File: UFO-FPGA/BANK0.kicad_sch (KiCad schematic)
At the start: 7 parts, among them U1 ICE40HX8K-BG121

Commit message: PCB
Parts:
- TP8: footprint TestPoint:TestPoint_Keystone_5000-5004_Miniature -> TestPoint:TestPoint_Pad_1.5x1.5mm
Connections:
- net ADC-CS: no longer U1.A5 (IOT_207)
- net MISO: no longer U1.A4 (IOT_211)
- net PIN-1: no longer U1.A1 (IOT_225)
- net PIN-2: no longer U1.A3 (IOT_223)
- net PIN-3: no longer U1.A2 (IOT_222)
- net PIN-4: no longer U1.B3 (IOT_221)
- net PIN-5: no longer U1.B4 (IOT_219)
- net PIN-6: no longer U1.B6 (IOT_198_GBIN0)
- net PIN-7: no longer U1.B7 (IOT_197_GBIN1)
- net SCK: no longer U1.A6 (IOT_206)
- net +1V2 renamed +3V3
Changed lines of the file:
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@@
+    (stroke (width 0) (type default))
+  )
+  (wire (pts (xy 191.135 48.895) (xy 191.135 38.735))
     (stroke (width 0) (type default))
   )
@@
     (stroke (width 0) (type default))
   )
+  (wire (pts (xy 101.6 108.585) (xy 114.3 108.585))
+    (stroke (width 0) (type default))
+  )
   (wire (pts (xy 127 48.895) (xy 127 57.785))
     (stroke (width 0) (type default))
   )
-  (wire (pts (xy 101.6 108.585) (xy 114.3 108.585))
-    (stroke (width 0) (type default))
-  )
   (wire (pts (xy 160.02 56.515) (xy 148.59 56.515))
     (stroke (width 0) (type default))
@@
     (stroke (width 0) (type default))
   )
-  (wire (pts (xy 190.5 38.735) (xy 190.5 48.895))
+  (wire (pts (xy 190.5 48.895) (xy 191.135 48.895))
     (stroke (width 0) (type default))
   )
@@
     (effects (font (size 1.27 1.27)) (justify left bottom))
   )
-  (global_label "PIN-7" (shape input) (at 101.6 100.965 180) (fields_autoplaced)
-    (effects (font (size 1.27 1.27)) (justify right))
-    (property "Intersheetrefs" "${INTERSHEET_REFS}" (at 92.707 100.965 0)
-      (effects (font (size 1.27 1.27)) (justify right) hide)
-    )
-  )
-  (global_label "PIN-3" (shape input) (at 101.6 123.825 180) (fields_autoplaced)
-    (effects (font (size 1.27 1.27)) (justify right))
-    (property "Intersheetrefs" "${INTERSHEET_REFS}" (at 92.707 123.825 0)
-      (effects (font (size 1.27 1.27)) (justify right) hide)
-    )
-  )
-  (global_label "PIN-6" (shape input) (at 101.6 103.505 180) (fields_autoplaced)
-    (effects (font (size 1.27 1.27)) (justify right))
-    (property "Intersheetrefs" "${INTERSHEET_REFS}" (at 92.707 103.505 0)
-      (effects (font (size 1.27 1.27)) (justify right) hide)
-    )
-  )
-  (global_label "MISO" (shape input) (at 101.6 113.665 180) (fields_autoplaced)
-    (effects (font (size 1.27 1.27)) (justify right))
-    (property "Intersheetrefs" "${INTERSHEET_REFS}" (at 94.098 113.665 0)
-      (effects (font (size 1.27 1.27)) (justify right) hide)
-    )
-  )
-  (global_label "ADC-CS" (shape input) (at 101.6 108.585 180) (fields_autoplaced)
-    (effects (font (size 1.27 1.27)) (justify right))
-    (property "Intersheetrefs" "${INTERSHEET_REFS}" (at 91.0137 108.585 0)
-      (effects (font (size 1.27 1.27)) (justify right) hide)
-    )
-  )
-  (global_label "PIN-5" (shape input) (at 101.6 118.745 180) (fields_autoplaced)
-    (effects (font (size 1.27 1.27)) (justify right))
-    (property "Intersheetrefs" "${INTERSHEET_REFS}" (at 92.707 118.745 0)
-      (effects (font (size 1.27 1.27)) (justify right) hide)
-    )
-  )
-  (global_label "PIN-2" (shape input) (at 101.6 126.365 180) (fields_autoplaced)
-    (effects (font (size 1.27 1.27)) (justify right))
-    (property "Intersheetrefs" "${INTERSHEET_REFS}" (at 92.707 126.365 0)
-      (effects (font (size 1.27 1.27)) (justify right) hide)
-    )
-  )
-  (global_label "PIN-1" (shape input) (at 101.6 128.905 180) (fields_autoplaced)
-    (effects (font (size 1.27 1.27)) (justify right))
-    (property "Intersheetrefs" "${INTERSHEET_REFS}" (at 92.707 128.905 0)
-      (effects (font (size 1.27 1.27)) (justify right) hide)
-    )
-  )
-  (global_label "SCK" (shape input) (at 101.6 106.045 180) (fields_autoplaced)
-    (effects (font (size 1.27 1.27)) (justify right))
-    (property "Intersheetrefs" "${INTERSHEET_REFS}" (at 94.9447 106.045 0)
-      (effects (font (size 1.27 1.27)) (justify right) hide)
-    )
-  )
-  (global_label "PIN-4" (shape input) (at 101.6 121.285 180) (fields_autoplaced)
-    (effects (font (size 1.27 1.27)) (justify right))
-    (property "Intersheetrefs" "${INTERSHEET_REFS}" (at 92.707 121.285 0)
+  (global_label "PIN-7" (shape input) (at 92.71 100.965 180) (fields_autoplaced)
+    (effects (font (size 1.27 1.27)) (justify right))
+    (property "Intersheetrefs" "${INTERSHEET_REFS}" (at 83.817 100.965 0)
+      (effects (font (size 1.27 1.27)) (justify right) hide)
+    )
+  )
+  (global_label "PIN-3" (shape input) (at 92.71 123.825 180) (fields_autoplaced)
+    (effects (font (size 1.27 1.27)) (justify right))
+    (property "Intersheetrefs" "${INTERSHEET_REFS}" (at 83.817 123.825 0)
+      (effects (font (size 1.27 1.27)) (justify right) hide)
+    )
+  )
+  (global_label "PIN-6" (shape input) (at 92.71 103.505 180) (fields_autoplaced)
+    (effects (font (size 1.27 1.27)) (justify right))
+    (property "Intersheetrefs" "${INTERSHEET_REFS}" (at 83.817 103.505 0)
+      (effects (font (size 1.27 1.27)) (justify right) hide)
+    )
+  )
+  (global_label "MISO" (shape input) (at 92.71 113.665 180) (fields_autoplaced)
+    (effects (font (size 1.27 1.27)) (justify right))
+    (property "Intersheetrefs" "${INTERSHEET_REFS}" (at 85.208 113.665 0)
+      (effects (font (size 1.27 1.27)) (justify right) hide)
+    )
+  )
+  (global_label "ADC-CS" (shape input) (at 92.71 108.585 180) (fields_autoplaced)
+    (effects (font (size 1.27 1.27)) (justify right))
+    (property "Intersheetrefs" "${INTERSHEET_REFS}" (at 82.1237 108.585 0)
+      (effects (font (size 1.27 1.27)) (justify right) hide)
+    )
+  )
+  (global_label "PIN-5" (shape input) (at 92.71 118.745 180) (fields_autoplaced)
+    (effects (font (size 1.27 1.27)) (justify right))
+    (property "Intersheetrefs" "${INTERSHEET_REFS}" (at 83.817 118.745 0)
+      (effects (font (size 1.27 1.27)) (justify right) hide)
+    )
+  )
+  (global_label "PIN-2" (shape input) (at 92.71 126.365 180) (fields_autoplaced)
+    (effects (font (size 1.27 1.27)) (justify right))
+    (property "Intersheetrefs" "${INTERSHEET_REFS}" (at 83.817 126.365 0)
+      (effects (font (size 1.27 1.27)) (justify right) hide)
+    )
+  )
+  (global_label "PIN-1" (shape input) (at 92.71 128.905 180) (fields_autoplaced)
+    (effects (font (size 1.27 1.27)) (justify right))
+    (property "Intersheetrefs" "${INTERSHEET_REFS}" (at 83.817 128.905 0)
+      (effects (font (size 1.27 1.27)) (justify right) hide)
+    )
+  )
+  (global_label "SCK" (shape input) (at 92.71 106.045 180) (fields_autoplaced)
+    (effects (font (size 1.27 1.27)) (justify right))
+    (property "Intersheetrefs" "${INTERSHEET_REFS}" (at 86.0547 106.045 0)
+      (effects (font (size 1.27 1.27)) (justify right) hide)
+    )
+  )
+  (global_label "PIN-4" (shape input) (at 92.71 121.285 180) (fields_autoplaced)
+    (effects (font (size 1.27 1.27)) (justify right))
+    (property "Intersheetrefs" "${INTERSHEET_REFS}" (at 83.817 121.285 0)
       (effects (font (size 1.27 1.27)) (justify right) hide)
     )
@@
         (path "/de984c47-a4b3-4404-8f6d-5958f9d846d6"
           (reference "#PWR0101") (unit 1)
+        )
+      )
+    )
+  )
+  (symbol (lib_id "power:+3V3") (at 191.135 38.735 0) (unit 1)
+    (in_bom yes) (on_board yes) (dnp no) (fields_autoplaced)
+    (property "Reference" "#PWR062" (at 191.135 42.545 0)
+      (effects (font (size 1.27 1.27)) hide)
+    )
+    (property "Value" "+3V3" (at 191.135 35.2331 0)
+      (effects (font (size 1.27 1.27)))
+    )
+    (property "Footprint" "" (at 191.135 38.735 0)
+      (effects (font (size 1.27 1.27)) hide)
+    )
+    (property "Datasheet" "" (at 191.135 38.735 0)
+      (effects (font (size 1.27 1.27)) hide)
+    )
+    (pin "1")
+    (instances
+      (project "UFO-FPGA"
+        (path "/b3168f6a-c732-41d3-aeeb-d97dd2f1bb65/03eb349d-f783-448d-a9ad-735fd21dbf61"
+          (reference "#PWR062") (unit 1)
         )
       )
@@
     )
   )
-  (symbol (lib_id "power:+1V2") (at 190.5 38.735 0) (unit 1)
-    (in_bom yes) (on_board yes) (dnp no) (fields_autoplaced)
-    (property "Reference" "#PWR024" (at 190.5 42.545 0)
-      (effects (font (size 1.27 1.27)) hide)
-    )
-    (property "Value" "+1V2" (at 190.5 35.2331 0)
-      (effects (font (size 1.27 1.27)))
-    )
-    (property "Footprint" "" (at 190.5 38.735 0)
-      (effects (font (size 1.27 1.27)) hide)
-    )
-    (property "Datasheet" "" (at 190.5 38.735 0)
-      (effects (font (size 1.27 1.27)) hide)
-    )
-    (pin "1")
-    (instances
-      (project "UFO-FPGA"
-        (path "/b3168f6a-c732-41d3-aeeb-d97dd2f1bb65/a9a0295d-b075-4952-a5ba-04debc5f691c"
-          (reference "#PWR024") (unit 1)
-        )
-        (path "/b3168f6a-c732-41d3-aeeb-d97dd2f1bb65/03eb349d-f783-448d-a9ad-735fd21dbf61"
-          (reference "#PWR076") (unit 1)
-        )
-        (path "/b3168f6a-c732-41d3-aeeb-d97dd2f1bb65/6f7e0d88-d92b-4c4f-9dc8-64721cd46d41"
-          (reference "#PWR029") (unit 1)
-        )
-        (path "/b3168f6a-c732-41d3-aeeb-d97dd2f1bb65/f54d4357-d916-4d6b-afb9-9dd5f65d1cf7"
-          (reference "#PWR036") (unit 1)
-        )
-      )
-      (project "BANK0"
-        (path "/de984c47-a4b3-4404-8f6d-5958f9d846d6"
-          (reference "#PWR024") (unit 1)
-        )
-      )
-    )
-  )
   (symbol (lib_id "Connector:TestPoint") (at 172.72 48.895 0) (unit 1)
     (in_bom yes) (on_board yes) (dnp no)
@@
       (effects (font (size 1.27 1.27)) (justify left))
     )
-    (property "Footprint" "TestPoint:TestPoint_Keystone_5000-5004_Miniature" (at 177.8 48.895 0)
-      (effects (font (size 1.27 1.27)) hide)
-    )
+    (property "Footprint" "TestPoint:TestPoint_Pad_1.5x1.5mm" (at 177.8 48.895 0)
+      (effects (font (size 1.27 1.27)) hide)
+    )

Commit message: PCB
many pcb changes
-started routing
-added vias
-power planes
-ground planes
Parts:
- removed C17 (x2): 100nF, Capacitor_SMD:C_0805_2012Metric_Pad1.18x1.45mm_HandSolder, symbol Device:C
- removed R25: 1, Resistor_SMD:R_0805_2012Metric_Pad1.20x1.40mm_HandSolder, symbol Device:R
- added R29: 0, Resistor_SMD:R_0805_2012Metric_Pad1.20x1.40mm_HandSolder, symbol Device:R
- C17, C18: value 100nF -> 200nF
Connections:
- net +3V3: now also R29.2
- net VCCIO_0: now also R29.1
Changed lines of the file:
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@@
   (junction (at 171.45 48.895) (diameter 0) (color 0 0 0 0)
   )
-  (junction (at 160.02 56.515) (diameter 0) (color 0 0 0 0)
-  )
-  (junction (at 148.59 48.895) (diameter 0) (color 0 0 0 0)
-  )
   (junction (at 172.72 48.895) (diameter 0) (color 0 0 0 0)
-  )
-  (junction (at 137.16 48.895) (diameter 0) (color 0 0 0 0)
-  )
-  (junction (at 148.59 56.515) (diameter 0) (color 0 0 0 0)
   )
   (no_connect (at 114.3 90.805))
@@
     (stroke (width 0) (type default))
   )
+  (wire (pts (xy 187.96 48.895) (xy 191.135 48.895))
+    (stroke (width 0) (type default))
+  )
   (wire (pts (xy 101.6 100.965) (xy 114.3 100.965))
     (stroke (width 0) (type default))
@@
     (stroke (width 0) (type default))
   )
-  (wire (pts (xy 160.02 56.515) (xy 148.59 56.515))
-    (stroke (width 0) (type default))
-  )
-  (wire (pts (xy 148.59 56.515) (xy 137.16 56.515))
-    (stroke (width 0) (type default))
-  )
   (wire (pts (xy 101.6 113.665) (xy 114.3 113.665))
     (stroke (width 0) (type default))
@@
     (stroke (width 0) (type default))
   )
-  (wire (pts (xy 190.5 48.895) (xy 191.135 48.895))
+  (wire (pts (xy 172.72 48.895) (xy 180.34 48.895))
     (stroke (width 0) (type default))
   )
@@
     (stroke (width 0) (type default))
   )
-  (wire (pts (xy 148.59 48.895) (xy 137.16 48.895))
-    (stroke (width 0) (type default))
-  )
-  (wire (pts (xy 137.16 48.895) (xy 127 48.895))
-    (stroke (width 0) (type default))
-  )
-  (wire (pts (xy 160.02 48.895) (xy 148.59 48.895))
-    (stroke (width 0) (type default))
-  )
-  (wire (pts (xy 172.72 48.895) (xy 182.88 48.895))
+  (wire (pts (xy 127 48.895) (xy 160.02 48.895))
     (stroke (width 0) (type default))
   )
@@
     (property "Intersheetrefs" "${INTERSHEET_REFS}" (at 83.817 121.285 0)
       (effects (font (size 1.27 1.27)) (justify right) hide)
-    )
-  )
-  (symbol (lib_id "Device:C") (at 148.59 52.705 0) (mirror y) (unit 1)
-    (in_bom yes) (on_board yes) (dnp no) (fields_autoplaced)
-    (property "Reference" "C17" (at 145.669 52.0613 0)
-      (effects (font (size 1.27 1.27)) (justify left))
-    )
-    (property "Value" "100nF" (at 145.669 53.9823 0)
-      (effects (font (size 1.27 1.27)) (justify left))
-    )
-    (property "Footprint" "Capacitor_SMD:C_0805_2012Metric_Pad1.18x1.45mm_HandSolder" (at 147.6248 56.515 0)
-      (effects (font (size 1.27 1.27)) hide)
-    )
-    (property "Datasheet" "~" (at 148.59 52.705 0)
-      (effects (font (size 1.27 1.27)) hide)
-    )
-    (pin "1")
-    (pin "2")
-    (instances
-      (project "UFO-FPGA"
-        (path "/b3168f6a-c732-41d3-aeeb-d97dd2f1bb65/a9a0295d-b075-4952-a5ba-04debc5f691c"
-          (reference "C17") (unit 1)
-        )
-        (path "/b3168f6a-c732-41d3-aeeb-d97dd2f1bb65/6f7e0d88-d92b-4c4f-9dc8-64721cd46d41"
-          (reference "C23") (unit 1)
-        )
-        (path "/b3168f6a-c732-41d3-aeeb-d97dd2f1bb65/f54d4357-d916-4d6b-afb9-9dd5f65d1cf7"
-          (reference "C26") (unit 1)
-        )
-        (path "/b3168f6a-c732-41d3-aeeb-d97dd2f1bb65/03eb349d-f783-448d-a9ad-735fd21dbf61"
-          (reference "C30") (unit 1)
-        )
-      )
-      (project "BANK0"
-        (path "/de984c47-a4b3-4404-8f6d-5958f9d846d6"
-          (reference "C17") (unit 1)
-        )
-      )
     )
   )
@@
       (effects (font (size 1.27 1.27)) (justify left))
     )
-    (property "Value" "100nF" (at 157.099 53.9823 0)
+    (property "Value" "200nF" (at 157.099 53.9823 0)
       (effects (font (size 1.27 1.27)) (justify left))
     )
@@
     )
   )
-  (symbol (lib_id "Device:R") (at 186.69 48.895 270) (unit 1)
-    (in_bom yes) (on_board yes) (dnp no)
-    (property "Reference" "R25" (at 186.69 52.9209 90)
+  (symbol (lib_id "Device:R") (at 184.15 48.895 90) (unit 1)
+    (in_bom yes) (on_board yes) (dnp no) (fields_autoplaced)
+    (property "Reference" "R29" (at 184.15 44.8691 90)
       (effects (font (size 1.27 1.27)))
     )
-    (property "Value" "1" (at 186.69 50.9999 90)
+    (property "Value" "0" (at 184.15 46.7901 90)
       (effects (font (size 1.27 1.27)))
     )
-    (property "Footprint" "Resistor_SMD:R_0805_2012Metric_Pad1.20x1.40mm_HandSolder" (at 186.69 47.117 90)
-      (effects (font (size 1.27 1.27)) hide)
-    )
-    (property "Datasheet" "~" (at 186.69 48.895 0)
+    (property "Footprint" "Resistor_SMD:R_0805_2012Metric_Pad1.20x1.40mm_HandSolder" (at 184.15 50.673 90)
+      (effects (font (size 1.27 1.27)) hide)
+    )
+    (property "Datasheet" "~" (at 184.15 48.895 0)
       (effects (font (size 1.27 1.27)) hide)
     )
@@
     (instances
       (project "UFO-FPGA"
-        (path "/b3168f6a-c732-41d3-aeeb-d97dd2f1bb65/a9a0295d-b075-4952-a5ba-04debc5f691c"
-          (reference "R25") (unit 1)
-        )
-        (path "/b3168f6a-c732-41d3-aeeb-d97dd2f1bb65/6f7e0d88-d92b-4c4f-9dc8-64721cd46d41"
-          (reference "R28") (unit 1)
-        )
         (path "/b3168f6a-c732-41d3-aeeb-d97dd2f1bb65/f54d4357-d916-4d6b-afb9-9dd5f65d1cf7"
-          (reference "R30") (unit 1)
-        )
-        (path "/b3168f6a-c732-41d3-aeeb-d97dd2f1bb65/03eb349d-f783-448d-a9ad-735fd21dbf61"
-          (reference "R31") (unit 1)
-        )
-      )
-      (project "BANK0"
-        (path "/de984c47-a4b3-4404-8f6d-5958f9d846d6"
-          (reference "R25") (unit 1)
+          (reference "R29") (unit 1)
+        )
+        (path "/b3168f6a-c732-41d3-aeeb-d97dd2f1bb65/03eb349d-f783-448d-a9ad-735fd21dbf61"
+          (reference "R32") (unit 1)
         )
       )
@@
       (effects (font (size 1.27 1.27)) (justify left))
     )
-    (property "Value" "100nF" (at 168.529 53.9823 0)
+    (property "Value" "200nF" (at 168.529 53.9823 0)
       (effects (font (size 1.27 1.27)) (justify left))
     )
@@
         )
       )
-    )
-  )
-  (symbol (lib_id "Device:C") (at 137.16 52.705 0) (mirror y) (unit 1)
-    (in_bom yes) (on_board yes) (dnp no) (fields_autoplaced)
-    (property "Reference" "C17" (at 134.239 52.0613 0)
-      (effects (font (size 1.27 1.27)) (justify left))
-    )
-    (property "Value" "100nF" (at 134.239 53.9823 0)
-      (effects (font (size 1.27 1.27)) (justify left))
-    )
-    (property "Footprint" "Capacitor_SMD:C_0805_2012Metric_Pad1.18x1.45mm_HandSolder" (at 136.1948 56.515 0)
-      (effects (font (size 1.27 1.27)) hide)
-    )
-    (property "Datasheet" "~" (at 137.16 52.705 0)
-      (effects (font (size 1.27 1.27)) hide)
-    )
-    (pin "1")
-    (pin "2")
-    (instances
-      (project "UFO-FPGA"
-        (path "/b3168f6a-c732-41d3-aeeb-d97dd2f1bb65/a9a0295d-b075-4952-a5ba-04debc5f691c"
-          (reference "C17") (unit 1)
-        )
-        (path "/b3168f6a-c732-41d3-aeeb-d97dd2f1bb65/6f7e0d88-d92b-4c4f-9dc8-64721cd46d41"
-          (reference "C24") (unit 1)
-        )
-        (path "/b3168f6a-c732-41d3-aeeb-d97dd2f1bb65/f54d4357-d916-4d6b-afb9-9dd5f65d1cf7"
-          (reference "C25") (unit 1)
-        )
-        (path "/b3168f6a-c732-41d3-aeeb-d97dd2f1bb65/03eb349d-f783-448d-a9ad-735fd21dbf61"
-          (reference "C29") (unit 1)
-        )
-      )
-      (project "BANK0"
-        (path "/de984c47-a4b3-4404-8f6d-5958f9d846d6"
-          (reference "C17") (unit 1)
-        )
-      )

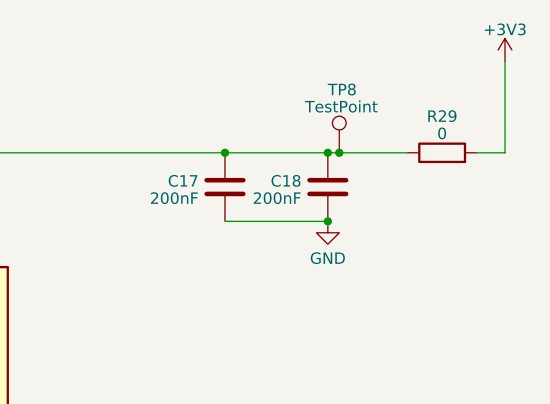
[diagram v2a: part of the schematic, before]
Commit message: pcb placement
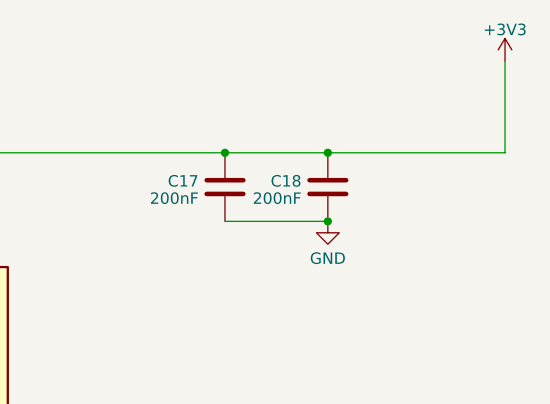
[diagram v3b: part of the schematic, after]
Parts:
- removed R29: 0, Resistor_SMD:R_0805_2012Metric_Pad1.20x1.40mm_HandSolder, symbol Device:R
- removed TP8: TestPoint, TestPoint:TestPoint_Pad_1.5x1.5mm, symbol Connector:TestPoint
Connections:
- net VCCIO_0 is gone; now on net +3V3: C17.1, C18.1, U1.D6 (VCCIO_0)
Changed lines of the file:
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@@
   (junction (at 171.45 48.895) (diameter 0) (color 0 0 0 0)
-  )
-  (junction (at 172.72 48.895) (diameter 0) (color 0 0 0 0)
   )
   (no_connect (at 114.3 90.805))
@@
     (stroke (width 0) (type default))
   )
-  (wire (pts (xy 187.96 48.895) (xy 191.135 48.895))
-    (stroke (width 0) (type default))
-  )
   (wire (pts (xy 101.6 100.965) (xy 114.3 100.965))
     (stroke (width 0) (type default))
@@
     (stroke (width 0) (type default))
   )
-  (wire (pts (xy 172.72 48.895) (xy 171.45 48.895))
+  (wire (pts (xy 171.45 48.895) (xy 191.135 48.895))
     (stroke (width 0) (type default))
   )
   (wire (pts (xy 101.6 121.285) (xy 114.3 121.285))
-    (stroke (width 0) (type default))
-  )
-  (wire (pts (xy 172.72 48.895) (xy 180.34 48.895))
     (stroke (width 0) (type default))
   )
@@
         )
       )
-    )
-  )
-  (symbol (lib_id "Connector:TestPoint") (at 172.72 48.895 0) (unit 1)
-    (in_bom yes) (on_board yes) (dnp no)
-    (property "Reference" "TP8" (at 171.45 41.91 0)
-      (effects (font (size 1.27 1.27)) (justify left))
-    )
-    (property "Value" "TestPoint" (at 168.91 43.815 0)
-      (effects (font (size 1.27 1.27)) (justify left))
-    )
-    (property "Footprint" "TestPoint:TestPoint_Pad_1.5x1.5mm" (at 177.8 48.895 0)
-      (effects (font (size 1.27 1.27)) hide)
-    )
-    (property "Datasheet" "~" (at 177.8 48.895 0)
-      (effects (font (size 1.27 1.27)) hide)
-    )
-    (pin "1")
-    (instances
-      (project "UFO-FPGA"
-        (path "/b3168f6a-c732-41d3-aeeb-d97dd2f1bb65/6f7e0d88-d92b-4c4f-9dc8-64721cd46d41"
-          (reference "TP8") (unit 1)
-        )
-        (path "/b3168f6a-c732-41d3-aeeb-d97dd2f1bb65/a9a0295d-b075-4952-a5ba-04debc5f691c"
-          (reference "TP5") (unit 1)
-        )
-        (path "/b3168f6a-c732-41d3-aeeb-d97dd2f1bb65/f54d4357-d916-4d6b-afb9-9dd5f65d1cf7"
-          (reference "TP9") (unit 1)
-        )
-        (path "/b3168f6a-c732-41d3-aeeb-d97dd2f1bb65/03eb349d-f783-448d-a9ad-735fd21dbf61"
-          (reference "TP10") (unit 1)
-        )
-      )
-      (project "BANK0"
-        (path "/de984c47-a4b3-4404-8f6d-5958f9d846d6"
-          (reference "TP8") (unit 1)
-        )
-      )
-    )
-  )
-  (symbol (lib_id "Device:R") (at 184.15 48.895 90) (unit 1)
-    (in_bom yes) (on_board yes) (dnp no) (fields_autoplaced)
-    (property "Reference" "R29" (at 184.15 44.8691 90)
-      (effects (font (size 1.27 1.27)))
-    )
-    (property "Value" "0" (at 184.15 46.7901 90)
-      (effects (font (size 1.27 1.27)))
-    )
-    (property "Footprint" "Resistor_SMD:R_0805_2012Metric_Pad1.20x1.40mm_HandSolder" (at 184.15 50.673 90)
-      (effects (font (size 1.27 1.27)) hide)
-    )
-    (property "Datasheet" "~" (at 184.15 48.895 0)
-      (effects (font (size 1.27 1.27)) hide)
-    )
-    (pin "1")
-    (pin "2")
-    (instances
-      (project "UFO-FPGA"
-        (path "/b3168f6a-c732-41d3-aeeb-d97dd2f1bb65/f54d4357-d916-4d6b-afb9-9dd5f65d1cf7"
-          (reference "R29") (unit 1)
-        )
-        (path "/b3168f6a-c732-41d3-aeeb-d97dd2f1bb65/03eb349d-f783-448d-a9ad-735fd21dbf61"
-          (reference "R32") (unit 1)
-        )
-      )

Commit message: pcb 0603
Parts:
- C17, C18: footprint Capacitor_SMD:C_0805_2012Metric_Pad1.18x1.45mm_HandSolder -> Capacitor_SMD:C_0603_1608Metric_Pad1.08x0.95mm_HandSolder
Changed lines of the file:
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@@
       (effects (font (size 1.27 1.27)) (justify left))
     )
-    (property "Footprint" "Capacitor_SMD:C_0805_2012Metric_Pad1.18x1.45mm_HandSolder" (at 159.0548 56.515 0)
+    (property "Footprint" "Capacitor_SMD:C_0603_1608Metric_Pad1.08x0.95mm_HandSolder" (at 159.0548 56.515 0)
       (effects (font (size 1.27 1.27)) hide)
     )
@@
       (effects (font (size 1.27 1.27)) (justify left))
     )
-    (property "Footprint" "Capacitor_SMD:C_0805_2012Metric_Pad1.18x1.45mm_HandSolder" (at 170.4848 56.515 0)
+    (property "Footprint" "Capacitor_SMD:C_0603_1608Metric_Pad1.08x0.95mm_HandSolder" (at 170.4848 56.515 0)
       (effects (font (size 1.27 1.27)) hide)
     )

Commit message: pcb
added John zendong
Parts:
- removed U1: ICE40HX8K-BG121, Package_BGA:BGA-121_9.0x9.0mm_Layout11x11_P0.8mm_Ball0.4mm_Pad0.35mm_NSMD, symbol FPGA_Lattice:ICE40HX8K-BG121
- added U4: ICE40HX4K-TQ144, Package_QFP:TQFP-144_20x20mm_P0.5mm, symbol FPGA_Lattice:ICE40HX4K-TQ144
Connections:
- net +3V3: now also U4.123 (VCCIO_0), U4.131 (VCCIO_0)
